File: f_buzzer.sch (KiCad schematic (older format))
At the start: 9 parts, among them U1 SN74123N

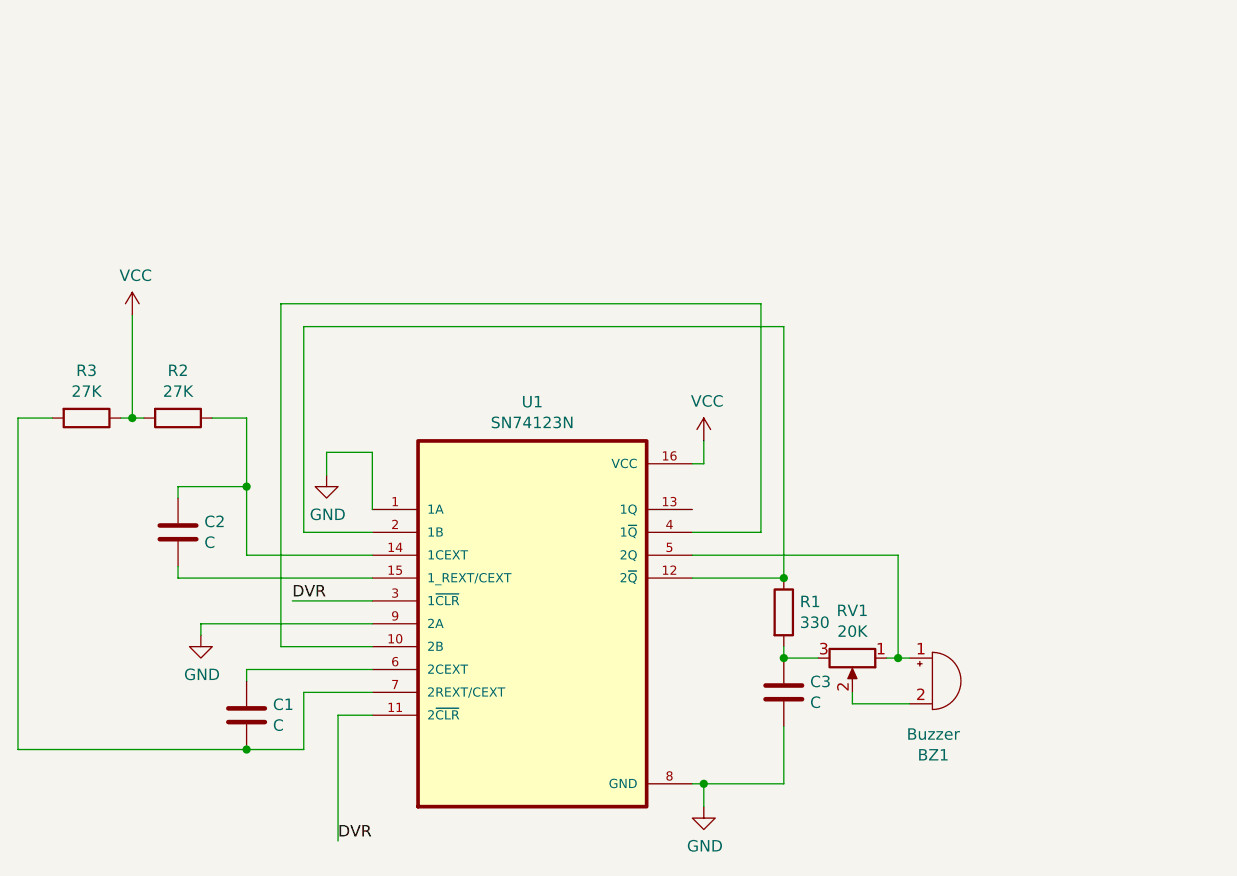
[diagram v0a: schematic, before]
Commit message: Fixed connections in schematic
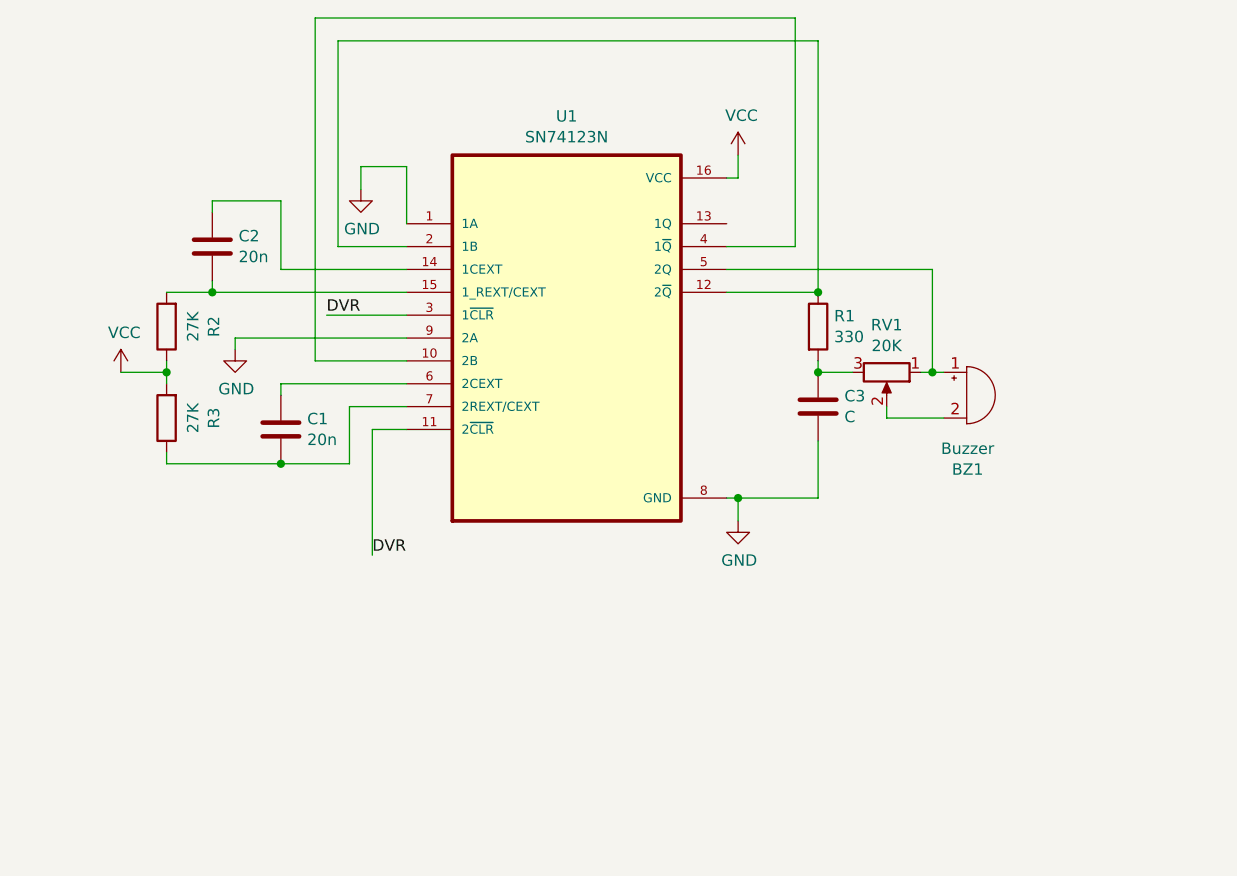
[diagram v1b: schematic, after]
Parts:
- C1, C2: value C -> 20n
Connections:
- net VCC: now also R2.1, R3.2; no longer R2.2, R3.1
- net at C1.2, U1.7 (2REXT/CEXT): now also R3.1; no longer R3.2
- net at C2.1, U1.14 (1CEXT): no longer R2.1
- net at C2.2, U1.15 (1_REXT/CEXT): now also R2.2
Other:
- moved on the sheet: BZ1, C1, C2, C3, R1, R2, R3, RV1, U1

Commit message: Added some constraints related to the case
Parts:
- BZ1: footprint Buzzer_Beeper:Buzzer_15x7.5RM7.6 -> Buzzer_Beeper:Buzzer_D14mm_H7mm_P10mm
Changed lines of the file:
@@
 F 0 "BZ1" H 7504 3975 50  0000 C CNN
 F 1 "Buzzer" H 7504 4066 50  0000 C CNN
-F 2 "Buzzer_Beeper:Buzzer_15x7.5RM7.6" V 7475 4400 50  0001 C CNN
+F 2 "Buzzer_Beeper:Buzzer_D14mm_H7mm_P10mm" V 7475 4400 50  0001 C CNN
 F 3 "~" V 7475 4400 50  0001 C CNN
 	1    7500 4300
@@
 	5050 3650 4750 3650
 Wire Wire Line
-	4750 3650 4750 2750
+	4750 3650 4750 2950
 $Comp
 L power:GND #PWR0105
@@
 	6450 3850 6850 3850
 Wire Wire Line
-	6850 2750 6850 3850
-Wire Wire Line
-	4750 2750 6850 2750
+	4750 2950 6850 2950
 Connection ~ 6850 3850
 Wire Wire Line
@@
 	5050 4150 4650 4150
 Wire Wire Line
-	4650 4150 4650 2650
+	4650 4150 4650 2850
 Wire Wire Line
-	4650 2650 6750 2650
-Wire Wire Line
-	6750 2650 6750 3650
+	4650 2850 6750 2850
 Wire Wire Line
 	6450 3650 6750 3650
@@
 Wire Wire Line
 	4000 4200 4000 4150
+Wire Wire Line
+	6850 2950 6850 3850
+Wire Wire Line
+	6750 2850 6750 3650
 $EndSCHEMATC

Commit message: Replaced the buzzer with the 22mm generic one
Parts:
- BZ1: footprint Buzzer_Beeper:Buzzer_D14mm_H7mm_P10mm -> f_buzzer:buzzer_front
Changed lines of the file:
@@
 F 0 "BZ1" H 7504 3975 50  0000 C CNN
 F 1 "Buzzer" H 7504 4066 50  0000 C CNN
-F 2 "Buzzer_Beeper:Buzzer_D14mm_H7mm_P10mm" V 7475 4400 50  0001 C CNN
+F 2 "f_buzzer:buzzer_front" V 7475 4400 50  0001 C CNN
 F 3 "~" V 7475 4400 50  0001 C CNN
 	1    7500 4300

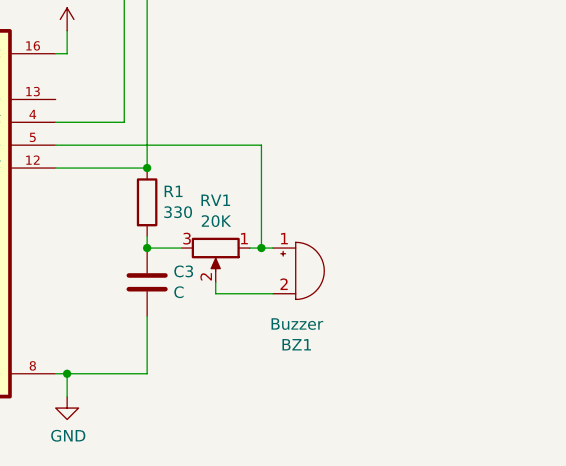
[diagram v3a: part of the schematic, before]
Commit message: Placed the two buzzers for 3D rendering of the board
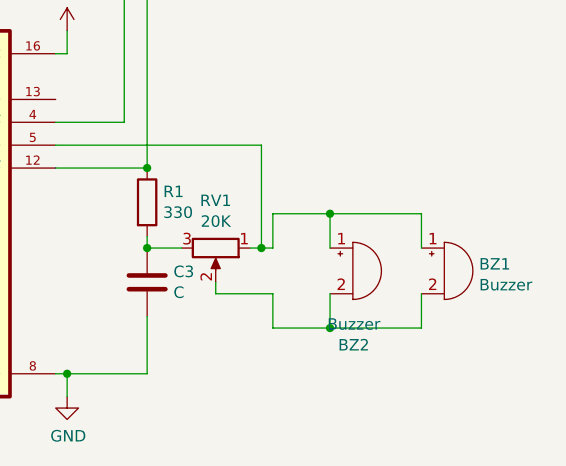
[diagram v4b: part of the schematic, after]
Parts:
- added BZ1: Buzzer, f_buzzer:buzzer_bottom, symbol Device:Buzzer
- renumbered BZ1 to BZ2
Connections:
- net at BZ2.1 (-), RV1.1, U1.5 (2Q): now also BZ1.1 (-)
- net at BZ2.2 (+), RV1.2: now also BZ1.2 (+)
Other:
- moved on the sheet: BZ2
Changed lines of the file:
@@
 Connection ~ 6500 4750
 $Comp
-L Device:Buzzer BZ1
+L Device:Buzzer BZ2
 U 1 1 601E9244
-P 7500 4300
-F 0 "BZ1" H 7504 3975 50  0000 C CNN
-F 1 "Buzzer" H 7504 4066 50  0000 C CNN
-F 2 "f_buzzer:buzzer_front" V 7475 4400 50  0001 C CNN
-F 3 "~" V 7475 4400 50  0001 C CNN
-	1    7500 4300
+P 7750 4300
+F 0 "BZ2" H 7754 3975 50  0000 C CNN
+F 1 "Buzzer" H 7754 4066 50  0000 C CNN
+F 2 "f_buzzer:buzzer_front" V 7725 4400 50  0001 C CNN
+F 3 "~" V 7725 4400 50  0001 C CNN
+	1    7750 4300
 	1    0    0    -1
 $EndComp
@@
 Wire Wire Line
 	6750 2850 6750 3650
+Wire Wire Line
+	7400 4200 7400 4050
+Wire Wire Line
+	7400 4050 7650 4050
+Wire Wire Line
+	8050 4050 8050 4200
+Wire Wire Line
+	7650 4200 7650 4050
+Connection ~ 7650 4050
+Wire Wire Line
+	7650 4050 8050 4050
+Wire Wire Line
+	7400 4400 7400 4550
+Wire Wire Line
+	7400 4550 7650 4550
+Wire Wire Line
+	8050 4550 8050 4400
+Wire Wire Line
+	7650 4400 7650 4550
+Connection ~ 7650 4550
+Wire Wire Line
+	7650 4550 8050 4550
+$Comp
+L Device:Buzzer BZ1
+U 1 1 602085CD
+P 8150 4300
+F 0 "BZ1" H 8302 4329 50  0000 L CNN
+F 1 "Buzzer" H 8302 4238 50  0000 L CNN
+F 2 "f_buzzer:buzzer_bottom" V 8125 4400 50  0001 C CNN
+F 3 "~" V 8125 4400 50  0001 C CNN
+	1    8150 4300
+	1    0    0    -1
+$EndComp
 $EndSCHEMATC

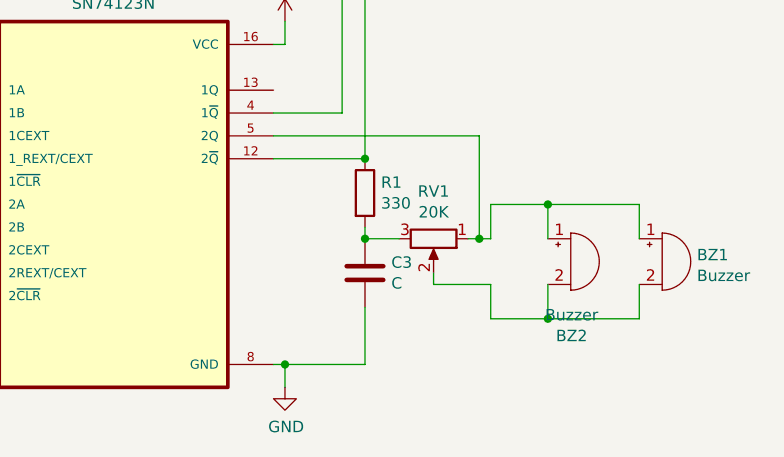
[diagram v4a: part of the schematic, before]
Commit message: Added C3 value to the schematic
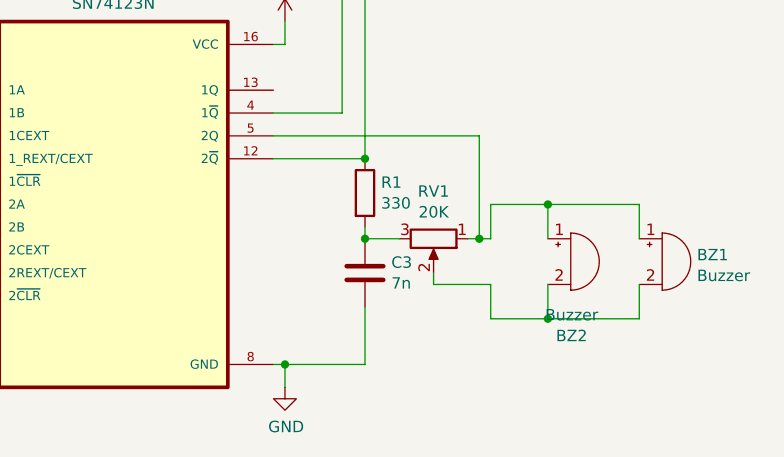
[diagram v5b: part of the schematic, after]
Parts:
- C3: value C -> 7n
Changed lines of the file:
@@
 P 6850 4350
 F 0 "C3" H 6965 4396 50  0000 L CNN
-F 1 "C" H 6965 4305 50  0000 L CNN
+F 1 "7n" H 6965 4305 50  0000 L CNN
 F 2 "Capacitor_THT:C_Disc_D5.1mm_W3.2mm_P5.00mm" H 6888 4200 50  0001 C CNN
 F 3 "~" H 6850 4350 50  0001 C CNN

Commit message: First SMD revision
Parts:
- removed U1: SN74123N, Package_DIP:DIP-16_W7.62mm, symbol SN74123N:SN74123N
- added U1: SN74LS123DRG4, f_buzzer:SN74LS123DRG4, symbol SN74123N:SN74LS123DRG4
- C1, C2: footprint Capacitor_THT:C_Disc_D5.1mm_W3.2mm_P5.00mm -> Capacitor_SMD:C_0603_1608Metric; JLCPCB (none) -> CL10B223KB8NNNC
- C3: footprint Capacitor_THT:C_Disc_D5.1mm_W3.2mm_P5.00mm -> Capacitor_SMD:C_0603_1608Metric; JLCPCB (none) -> 0603B682K500NT
- R1: footprint Resistor_THT:R_Axial_DIN0207_L6.3mm_D2.5mm_P7.62mm_Horizontal -> Resistor_SMD:R_0603_1608Metric; JLCPCB (none) -> 0603WAJ0331T5E
- R2, R3: footprint Resistor_THT:R_Axial_DIN0207_L6.3mm_D2.5mm_P7.62mm_Horizontal -> Resistor_SMD:R_0603_1608Metric; JLCPCB (none) -> 0603WAF2702T5E
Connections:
- net DVR: now also U1.11 (2~CLR), U1.3 (1~CLR)
- net GND: now also U1.1 (1A), U1.8 (GND), U1.9 (2A)
- net VCC: now also U1.16 (VCC)
- net at R1.1: now also U1.12 (2~Q), U1.2 (1B)
- net at C1.2, R3.1: now also U1.7 (2REXT/CEXT)
- net at C2.2, R2.2: now also U1.15 (1REXT/CEXT)
- net at C1.1: now also U1.6 (2CEXT)
- net at C2.1: now also U1.14 (1CEXT)
- net at BZ1.1 (-), BZ2.1 (-), RV1.1: now also U1.5 (2Q)
- new net: U1.10 (2B), U1.4 (1~Q)

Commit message: Added fill zones
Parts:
- C1, C2: JLCPCB CL10B223KB8NNNC -> (none); LCSC (none) -> C21122
- C3: JLCPCB 0603B682K500NT -> (none); LCSC (none) -> C1631
- R1: JLCPCB 0603WAJ0331T5E -> (none); LCSC (none) -> C25231
- R2, R3: JLCPCB 0603WAF2702T5E -> (none); LCSC (none) -> C22967
- U1: JLCPCB SN74LS123DRG4 -> (none); LCSC (none) -> C7733
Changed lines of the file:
@@
 F 2 "Resistor_SMD:R_0603_1608Metric" V 3930 4400 50  0001 C CNN
 F 3 "~" H 4000 4400 50  0001 C CNN
-F 4 "0603WAF2702T5E" V 4000 4400 50  0001 C CNN "JLCPCB"
+F 4 "C22967" V 4000 4400 50  0001 C CNN "LCSC"
 	1    4000 4400
 	-1   0    0    1
@@
 F 2 "Resistor_SMD:R_0603_1608Metric" V 3930 4000 50  0001 C CNN
 F 3 "~" H 4000 4000 50  0001 C CNN
-F 4 "0603WAF2702T5E" V 4000 4000 50  0001 C CNN "JLCPCB"
+F 4 "C22967" V 4000 4000 50  0001 C CNN "LCSC"
 	1    4000 4000
 	-1   0    0    1
@@
 F 2 "Capacitor_SMD:C_0603_1608Metric" H 4238 3500 50  0001 C CNN
 F 3 "~" H 4200 3650 50  0001 C CNN
-F 4 "CL10B223KB8NNNC" H 4200 3650 50  0001 C CNN "JLCPCB"
+F 4 "C21122" H 4200 3650 50  0001 C CNN "LCSC"
 	1    4200 3650
 	1    0    0    -1
@@
 F 2 "Capacitor_SMD:C_0603_1608Metric" H 4538 4300 50  0001 C CNN
 F 3 "~" H 4500 4450 50  0001 C CNN
-F 4 "CL10B223KB8NNNC" H 4500 4450 50  0001 C CNN "JLCPCB"
+F 4 "C21122" H 4500 4450 50  0001 C CNN "LCSC"
 	1    4500 4450
 	1    0    0    -1
@@
 F 2 "Capacitor_SMD:C_0603_1608Metric" H 6888 4200 50  0001 C CNN
 F 3 "~" H 6850 4350 50  0001 C CNN
-F 4 "0603B682K500NT" H 6850 4350 50  0001 C CNN "JLCPCB"
+F 4 "C1631" H 6850 4350 50  0001 C CNN "LCSC"
 	1    6850 4350
 	1    0    0    -1
@@
 F 2 "Resistor_SMD:R_0603_1608Metric" V 6780 4000 50  0001 C CNN
 F 3 "~" H 6850 4000 50  0001 C CNN
-F 4 "0603WAJ0331T5E" H 6850 4000 50  0001 C CNN "JLCPCB"
+F 4 "C25231" H 6850 4000 50  0001 C CNN "LCSC"
 	1    6850 4000
 	1    0    0    -1
@@
 F 3 "https://www.ti.com/lit/ds/symlink/sn74123.pdf" H 5750 4050 50  0001 L BNN
 F 4 "Texas Instruments" H 5750 4050 50  0001 L BNN "Manufacturer"
-F 5 "SN74LS123DRG4" H 5750 4050 50  0001 C CNN "JLCPCB"
+F 5 " C7733" H 5750 4050 50  0001 C CNN "LCSC"
 	1    5750 4050
 	1    0    0    -1

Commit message: Updated the SN74LS123DRG4 footprint
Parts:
- R1: LCSC C25231 -> C23138
- U1: footprint f_buzzer:SN74LS123DRG4 -> Package_SO:SOIC-16_3.9x9.9mm_P1.27mm
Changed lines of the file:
@@
 F 2 "Resistor_SMD:R_0603_1608Metric" V 6780 4000 50  0001 C CNN
 F 3 "~" H 6850 4000 50  0001 C CNN
-F 4 "C25231" H 6850 4000 50  0001 C CNN "LCSC"
+F 4 "C23138" H 6850 4000 50  0001 C CNN "LCSC"
 	1    6850 4000
 	1    0    0    -1
@@
 F 0 "U1" H 5750 5020 50  0000 C CNN
 F 1 "SN74LS123DRG4" H 5750 4929 50  0000 C CNN
-F 2 "f_buzzer:SN74LS123DRG4" H 5750 4050 50  0001 L BNN
+F 2 "Package_SO:SOIC-16_3.9x9.9mm_P1.27mm" H 5750 4050 50  0001 L BNN
 F 3 "https://www.ti.com/lit/ds/symlink/sn74123.pdf" H 5750 4050 50  0001 L BNN
 F 4 "Texas Instruments" H 5750 4050 50  0001 L BNN "Manufacturer"
